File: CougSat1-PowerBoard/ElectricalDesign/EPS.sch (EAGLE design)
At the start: 250 parts, among them J1 PV0, J2 PV1, J3 PV2, J4 PV3, J5 Umbilical, J6 SWD, J7 CougSat Card, J8 Deployables, Q1 NTLUD3A50PZ, Q10 DMN2008LFU, Q11 DMN2008LFU, Q12 CSD25402Q3A, Q13 CSD25402Q3A, Q14 NTLUD3A50PZ, Q15 NTLUD3A50PZ, Q16 NTLUD3A50PZ, Q17 NTLUD3A50PZ, Q18 NTLUD3A50PZ, Q19 NTLUD3A50PZ, Q2 NTLUD3A50PZ, Q20 NTLUD3A50PZ, Q21 NTLUD3A50PZ, Q22 NTLUD3A50PZ, Q23 CSD25402Q3A, Q24 CSD25402Q3A, Q25 DMN53D0L, Q26 NTLUD3A50PZ, Q27 NTLUD3A50PZ, Q28 NTLUD3A50PZ, Q29 NTLUD3A50PZ, Q3 NTLUD3A50PZ, Q30 NTLUD3A50PZ, Q31 NTLUD3A50PZ, Q32 NTLUD3A50PZ, Q33 NTLUD3A50PZ, Q34 NTLUD3A50PZ, Q35 NTLUD3A50PZ, Q36 NTLUD3A50PZ, Q37 NTLUD3A50PZ, Q38 NTLUD3A50PZ, Q39 NTLUD3A50PZ, Q4 NTLUD3A50PZ, Q40 NTLUD3A50PZ, Q41 NTLUD3A50PZ, Q42 NTLUD3A50PZ, Q43 NTLUD3A50PZ, Q5 NTLUD3A50PZ, Q6 NTLUD3A50PZ, Q7 NTLUD3A50PZ, Q8 NTLUD3A50PZ, Q9 NTLUD3A50PZ, SW1 D2MQ-1-TL, U1 BQ29700, U10 LTC2499, U11 LTC2499, U12 LTC2499, U13 LTC2499, U14 MCP1501-18, U15 LTC2499, U2 BQ29700, U3 TPS64200, U4 TPS64200, U5 STM32L476RGT, U6 TCA9535R, U7 SN74LVC244AR, U8 TCA9535R, U9 LTC2499

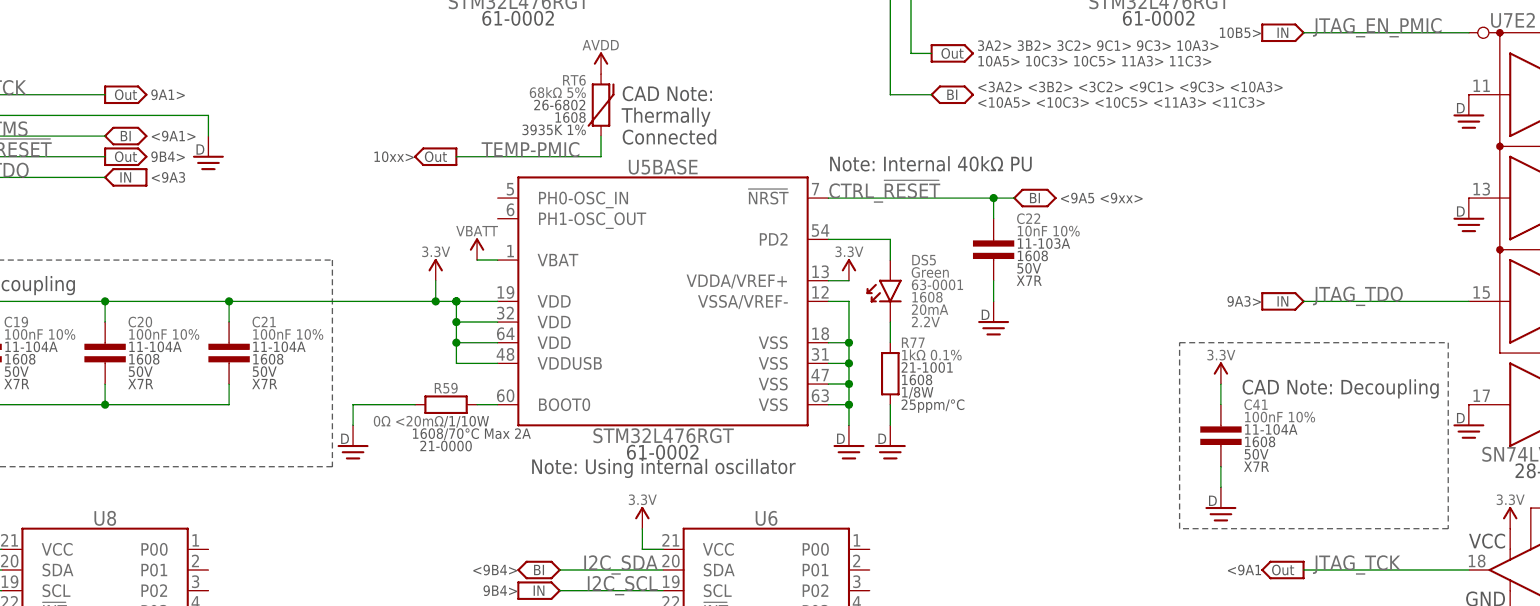
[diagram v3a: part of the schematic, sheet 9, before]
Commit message: Placed Components in Rough Location
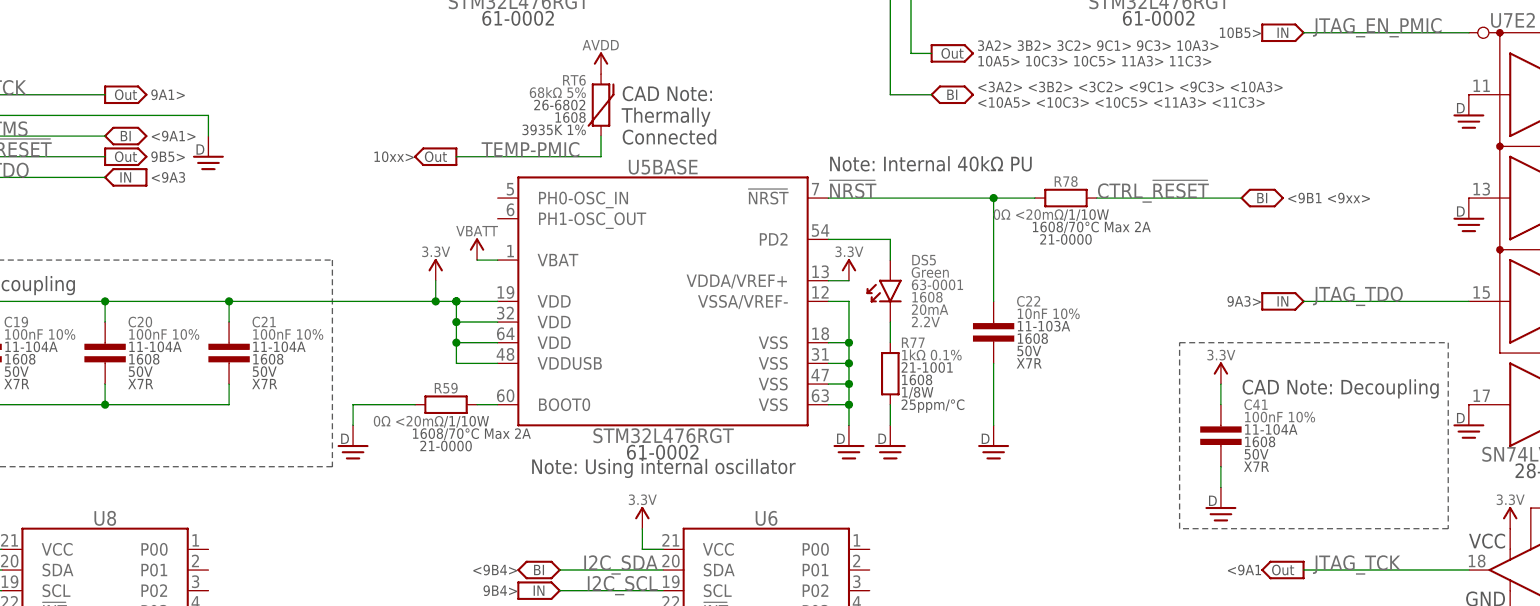
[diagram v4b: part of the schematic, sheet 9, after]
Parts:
- added LOGO1: Satellite 16mm, CougsInSpace-Aesthetics:CIS-LOGO-SATELLITE-16MM
- added LOGO2: SIGNATUREBRADLEY, CougsInSpace-Aesthetics:SIGNATUREBRADLEY
- added R78: 0Ω <20mΩ, CougsInSpace-Resistors:RES-H-0-1608
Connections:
- new net !NRST: C22.1, R78.1, U5BASE.!NRST
- net CTRL_!RESET: now also R78.2; no longer C22.1, U5BASE.!NRST
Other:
- note added: "9B5>"
- note added: "<9B1 <9xx>"
- note added: "<9B5>"
- note removed: "<9A5 <9xx>"
- moved on the sheet: C22
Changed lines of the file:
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@@
 <?xml version="1.0" encoding="utf-8"?>
 <!DOCTYPE eagle SYSTEM "eagle.dtd">
-<eagle version="9.1.1">
+<eagle version="9.1.2">
 <drawing>
 <settings>
@@
 <attribute name="PART_NUMBER" value="68-0002"/>
 <attribute name="PROJECT" value="CougSat-1: EPS"/>
-<attribute name="REV" value="2.1.2"/>
+<attribute name="REV" value="2.1.3"/>
 </attributes>
 <variantdefs>
@@
 <part name="SUPPLY164" library="CougsInSpace-PowerSymbols" deviceset="3.3V" device=""/>
 <part name="SUPPLY165" library="CougsInSpace-PowerSymbols" deviceset="3.3V" device=""/>
+<part name="R78" library="CougsInSpace-Resistors" deviceset="RES-H" device="-1608" technology="-0" value="0Ω &lt;20mΩ"/>
+<part name="LOGO1" library="CougsInSpace-Aesthetics" deviceset="CIS-LOGO" device="-SATELLITE-16MM" value="Satellite 16mm"/>
+<part name="LOGO2" library="CougsInSpace-Aesthetics" deviceset="SIGNATURE" device="BRADLEY"/>
 </parts>
 <sheets>
@@
 <text x="88.9" y="71.12" size="1.27" layer="97" align="center-right">9B4&gt; </text>
 <text x="43.18" y="132.08" size="1.27" layer="97" align="center-left"> 9A1&gt; </text>
-<text x="43.18" y="124.46" size="1.27" layer="97" align="center-left"> 9B4&gt;</text>
+<text x="43.18" y="124.46" size="1.27" layer="97" align="center-left"> 9B5&gt;</text>
 <text x="43.18" y="127" size="1.27" layer="97" align="center-left"> &lt;9A1&gt; </text>
 <text x="43.18" y="121.92" size="1.27" layer="97" align="center-left"> &lt;9A3</text>
@@
 <text x="43.18" y="147.32" size="1.27" layer="97" align="center-left"> &lt;9C5</text>
 <text x="121.92" y="177.8" size="1.27" layer="97" align="center-left"> 9B1&gt; 9B5&gt;</text>
-<text x="154.94" y="119.38" size="1.27" layer="97" align="center-left"> &lt;9A5 &lt;9xx&gt;</text>
+<text x="182.88" y="119.38" size="1.27" layer="97" align="center-left"> &lt;9B1 &lt;9xx&gt;</text>
 <text x="200.66" y="185.42" size="1.27" layer="97" align="center-left"> &lt;10B5</text>
 <text x="200.66" y="182.88" size="1.27" layer="97" align="center-left"> &lt;10B5&gt;</text>
@@
 <instance part="R59" gate="G$1" x="81.28" y="93.98"/>
 <instance part="SUPPLY41" gate="1" x="68.58" y="88.9"/>
-<instance part="C22" gate="G$1" x="147.32" y="111.76"/>
-<instance part="SUPPLY42" gate="1" x="147.32" y="104.14"/>
+<instance part="C22" gate="G$1" x="147.32" y="101.6"/>
+<instance part="SUPPLY42" gate="1" x="147.32" y="88.9"/>
 <instance part="SUPPLY43" gate="G$1" x="20.32" y="137.16"/>
 <instance part="SUPPLY44" gate="1" x="50.8" y="124.46"/>
@@
 <instance part="U7" gate="E1" x="213.36" y="73.66" rot="MR0"/>
 <instance part="U7" gate="E2" x="215.9" y="132.08"/>
-<instance part="OFFSHEET303" gate="G$1" x="152.4" y="119.38" rot="MR0"/>
+<instance part="OFFSHEET303" gate="G$1" x="180.34" y="119.38" rot="MR0"/>
 <instance part="RT6" gate="G$1" x="99.06" y="129.54" rot="MR0"/>
 <instance part="OFFSHEET383" gate="G$1" x="78.74" y="124.46"/>
@@
 <instance part="DS5" gate="G$1" x="134.62" y="106.68"/>
 <instance part="SUPPLY159" gate="1" x="134.62" y="88.9"/>
+<instance part="R78" gate="G$1" x="157.48" y="119.38"/>
 </instances>
 <busses>
@@
 <pinref part="C22" gate="G$1" pin="2"/>
 <pinref part="SUPPLY42" gate="1" pin="DGND"/>
-<wire x1="147.32" y1="109.22" x2="147.32" y2="106.68" width="0.1524" layer="91"/>
+<wire x1="147.32" y1="99.06" x2="147.32" y2="91.44" width="0.1524" layer="91"/>
 </segment>
 <segment>
@@
 <net name="CTRL_!RESET" class="0">
 <segment>
-<pinref part="U5" gate="BASE" pin="!NRST"/>
-<wire x1="127" y1="119.38" x2="147.32" y2="119.38" width="0.1524" layer="91"/>
-<pinref part="C22" gate="G$1" pin="1"/>
-<wire x1="147.32" y1="119.38" x2="147.32" y2="116.84" width="0.1524" layer="91"/>
-<junction x="147.32" y="119.38"/>
-<label x="127" y="119.38" size="1.778" layer="95"/>
-<wire x1="147.32" y1="119.38" x2="149.86" y2="119.38" width="0.1524" layer="91"/>
-</segment>
-<segment>
 <pinref part="J6" gate="G$1" pin="!RST"/>
 <wire x1="17.78" y1="124.46" x2="38.1" y2="124.46" width="0.1524" layer="91"/>
 <label x="17.78" y="124.46" size="1.778" layer="95"/>
 </segment>
+<segment>
+<pinref part="R78" gate="G$1" pin="2"/>
+<wire x1="160.02" y1="119.38" x2="177.8" y2="119.38" width="0.1524" layer="91"/>
+<label x="160.02" y="119.38" size="1.778" layer="95"/>
+</segment>
 </net>
 <net name="JTAG_TCK" class="0">
@@
 </segment>
 </net>
+<net name="!NRST" class="0">
+<segment>
+<pinref part="U5" gate="BASE" pin="!NRST"/>
+<wire x1="127" y1="119.38" x2="147.32" y2="119.38" width="0.1524" layer="91"/>
+<pinref part="C22" gate="G$1" pin="1"/>
+<wire x1="147.32" y1="119.38" x2="147.32" y2="106.68" width="0.1524" layer="91"/>
+<junction x="147.32" y="119.38"/>
+<label x="127" y="119.38" size="1.778" layer="95"/>
+<pinref part="R78" gate="G$1" pin="1"/>
+<wire x1="152.4" y1="119.38" x2="147.32" y2="119.38" width="0.1524" layer="91"/>
+</segment>
+</net>
 </nets>
 </sheet>
@@
 Note: All signals above are DS, connect to any DS input,
 whichever is best for routing, including the DS adc on page 10</text>
-<text x="200.66" y="83.82" size="1.27" layer="97" align="center-right">&lt;9B4&gt; </text>
+<text x="200.66" y="83.82" size="1.27" layer="97" align="center-right">&lt;9B5&gt; </text>
 <text x="200.66" y="109.22" size="1.27" layer="97" align="center-right">&lt;9A5&gt; </text>
 <text x="200.66" y="106.68" size="1.27" layer="97" align="center-right">&lt;9A5 </text>
@@
 <instance part="J7" gate="MECH-TOP" x="23" y="104"/>
 <instance part="J7" gate="MECH-BOTTOM" x="236" y="104" rot="MR0"/>
+<instance part="LOGO1" gate="G$1" x="15.24" y="22.86"/>
+<instance part="LOGO2" gate="G$1" x="12.7" y="12.7"/>
 </instances>
 <busses>

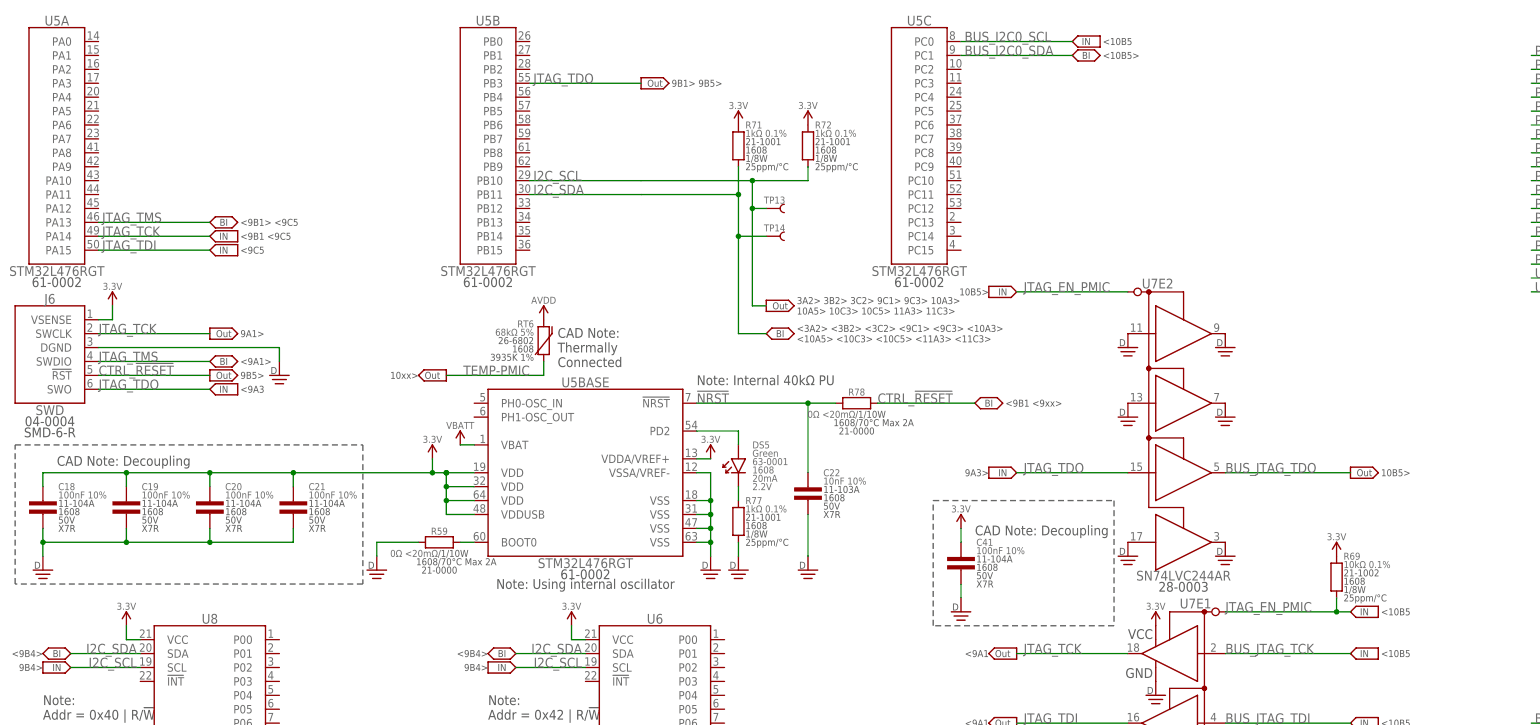
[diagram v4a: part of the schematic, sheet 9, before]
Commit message: Added JTAG Termintation and Regulator Gate Series Resistors
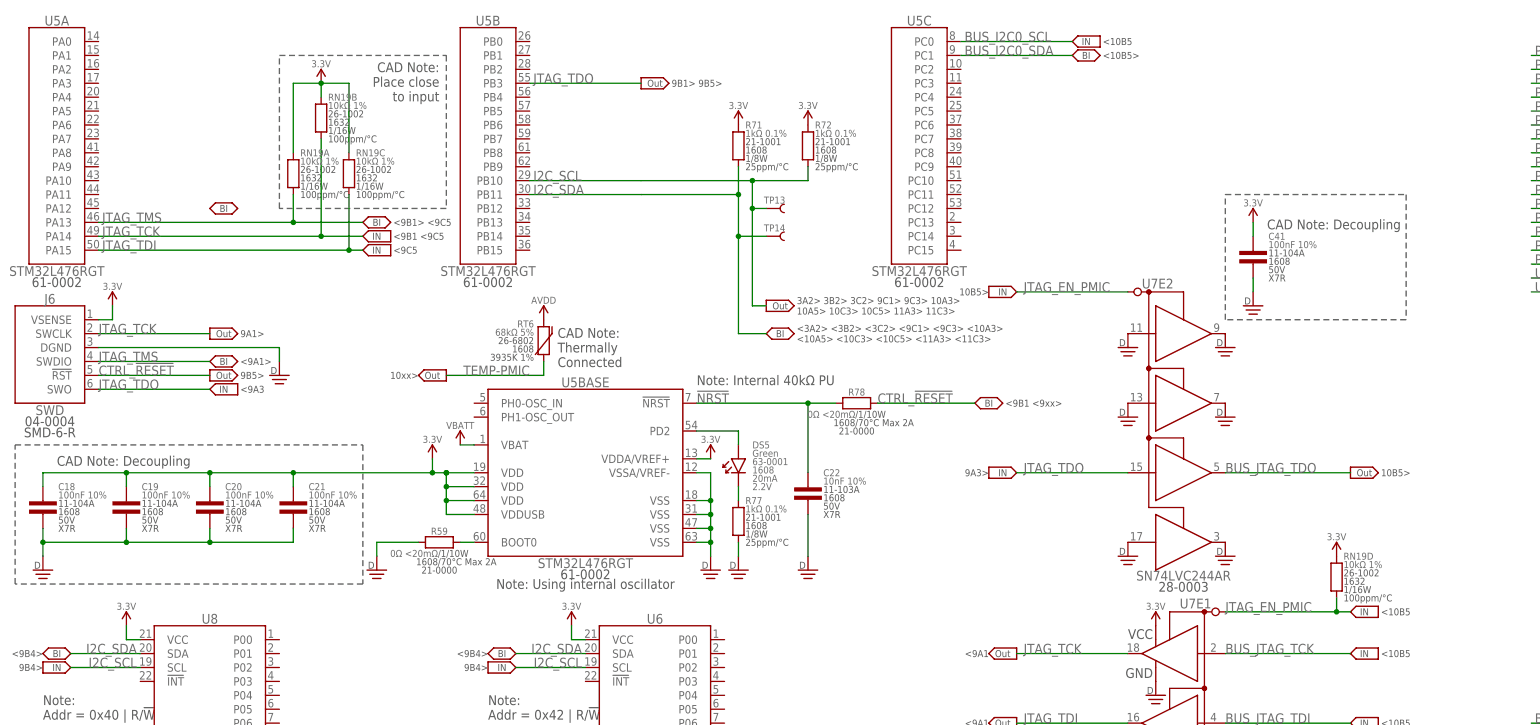
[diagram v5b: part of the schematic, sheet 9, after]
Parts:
- removed R69: 10kΩ 0.1%, CougsInSpace-Resistors:RES-V-10K-1608
- removed TP5, TP6, TP8, TP9: TEST_POINT-SMD-C-1.25, CougsInSpace-Connectors:TEST_POINT-SMD-C-1.25
- added R79, R80: 0Ω <20mΩ, CougsInSpace-Resistors:RES-H-0-1608
- added RN19: 10kΩ 1%, CougsInSpace-Resistors:RES-4-V-10K-1632
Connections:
- new net 3.3V_REG_SW_GATE-A: Q13.G, R79.2
- new net 3.3V_REG_SW_GATE-B: Q12.G, R80.2
- net 3.3V: now also RN19A.2, RN19B.2, RN19C.2, RN19D.2; no longer R69.2
- net 3.3V_REG_BUCK_NODE-A: no longer TP8.1
- net 3.3V_REG_BUCK_NODE-B: no longer TP5.1
- net 3.3V_REG_SW-A: now also R79.1; no longer Q13.G, TP9.1
- net 3.3V_REG_SW-B: now also R80.1; no longer Q12.G, TP6.1
- net JTAG_EN_PMIC: now also RN19D.1; no longer R69.1
- net JTAG_TCK: now also RN19B.1
- net JTAG_TDI: now also RN19C.1
- net JTAG_TMS: now also RN19A.1
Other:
- note added: "CAD Note: Place close to input"
- note added: "Note: Adjust gate resistor to optimize ringing and efficiency"
- moved on the sheet: C41

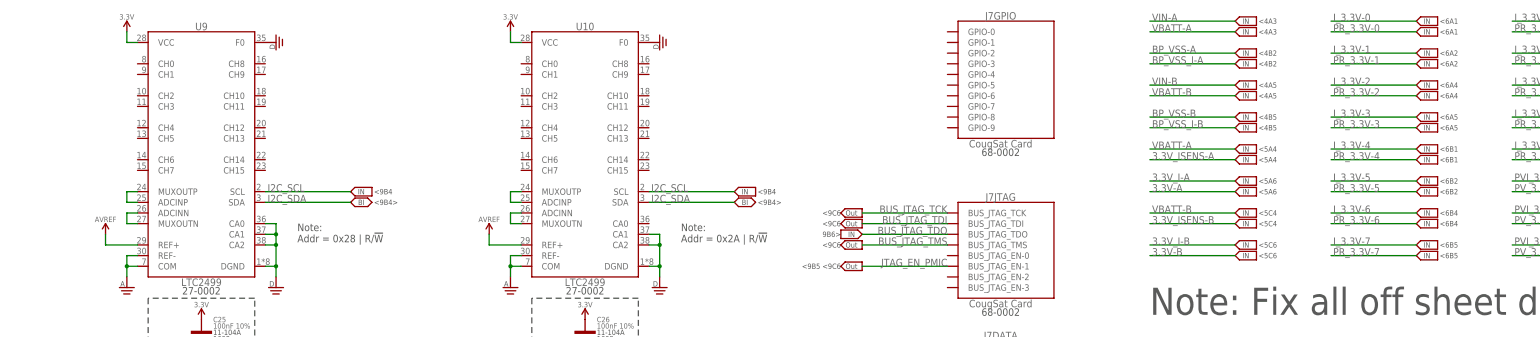
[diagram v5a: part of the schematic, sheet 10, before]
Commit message: Laid Out 3.3V Channels
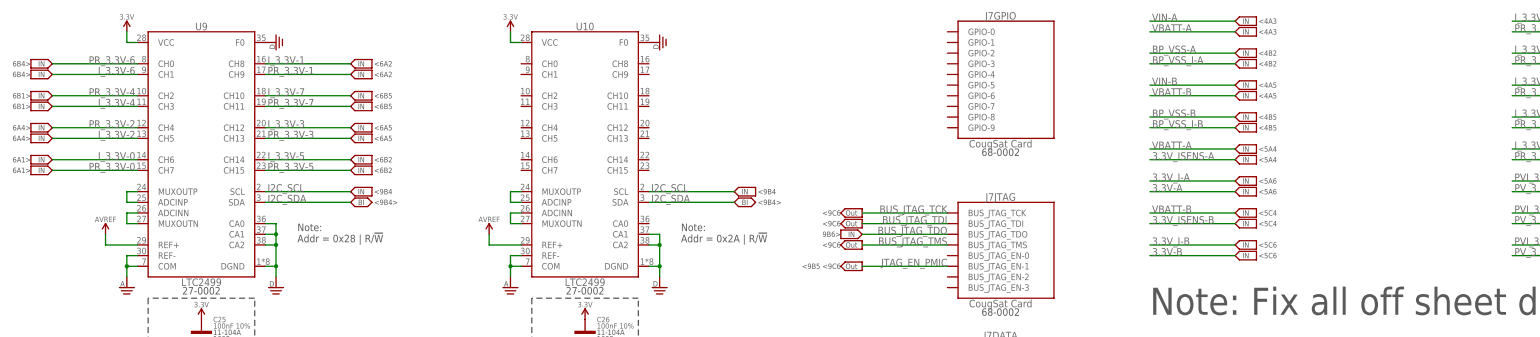
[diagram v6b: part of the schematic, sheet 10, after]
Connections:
- net I_3.3V-0: now also U9.CH6
- net I_3.3V-1: now also U9.CH8
- net I_3.3V-2: now also U9.CH5
- net I_3.3V-3: now also U9.CH12
- net I_3.3V-4: now also U9.CH3
- net I_3.3V-5: now also U9.CH14
- net I_3.3V-6: now also U9.CH1
- net I_3.3V-7: now also U9.CH10
- net PR_3.3V-0: now also U9.CH7
- net PR_3.3V-1: now also U9.CH9
- net PR_3.3V-2: now also U9.CH4
- net PR_3.3V-3: now also U9.CH13
- net PR_3.3V-4: now also U9.CH2
- net PR_3.3V-5: now also U9.CH15
- net PR_3.3V-6: now also U9.CH0
- net PR_3.3V-7: now also U9.CH11
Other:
- note added: "<10A1"
- note added: "<10A3"
- note added: "<6C5 <10A1"
- note added: "<6C5 <10A3"
- note removed: "<6A1"
- note removed: "<6A4"
- note removed: "<6B1"
- note removed: "<6B4"
